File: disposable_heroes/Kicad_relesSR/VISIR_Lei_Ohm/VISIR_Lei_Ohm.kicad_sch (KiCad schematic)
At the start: 23 parts, among them J1 Raspberry PI5, J2 Fonte dc, J3 Fonte 12V, J4 Fonte 5V, K1 3572-1220-123, K2 3572-1220-123, K3 3572-1220-123, K4 3570-1331-123, K5 3570-1331-123, K6 3572-1220-123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

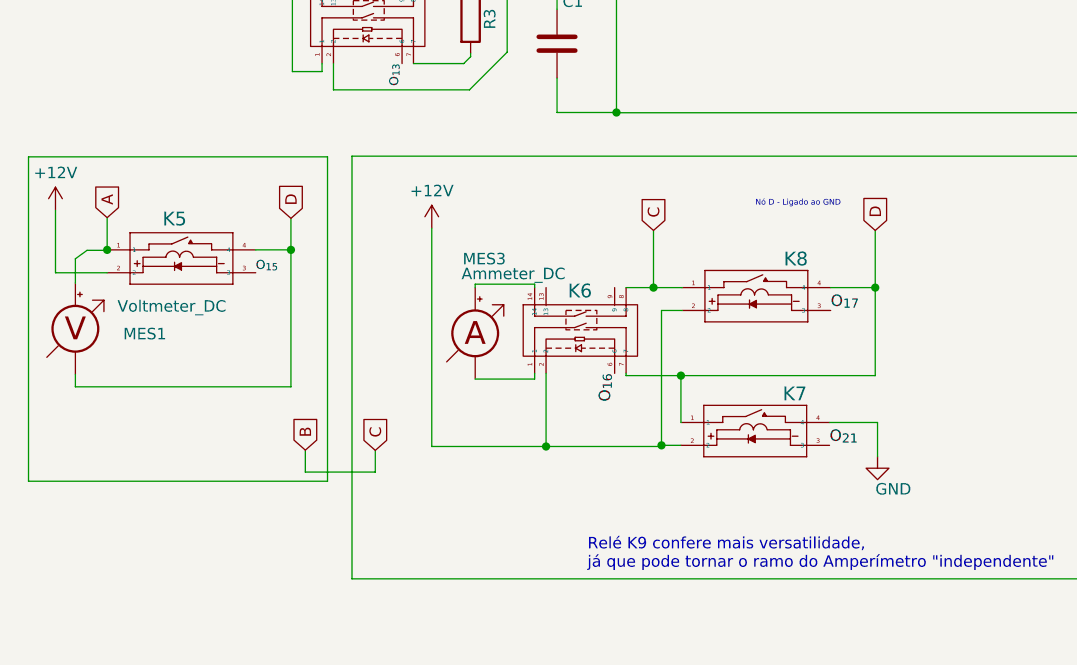
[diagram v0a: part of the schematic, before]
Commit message: Voltage/Current done Graphic interface NOT done
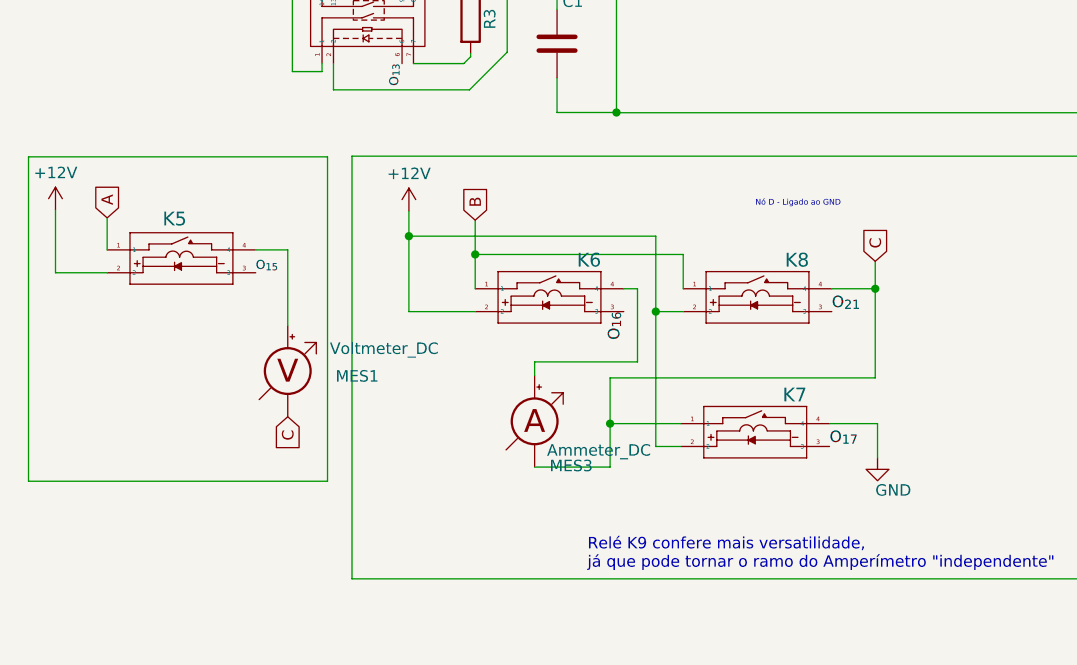
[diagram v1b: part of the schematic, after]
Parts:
- removed K6: 3572-1220-123, 3572-1220-053:RELAY8_3572-1220-053_COM, symbol 3572-1220-123:3572-1220-123
- added K6: 3570-1331-123, 3570-1220-123:SIP_3570-1331_COM, symbol 3570-1331-123:3570-1331-123
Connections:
- net +12V: now also K6.2
- net A: no longer MES1.2 (+)
- net B: now also K6.1
- net D: no longer K5.4, K7.1, K8.4, MES1.1 (-)
- net O_{16}: now also K6.3
- net O_{17}: now also K7.3; no longer K8.3
- net O_{21}: now also K8.3; no longer K7.3
- net C: now reaches MES3.1 (-)
- net C: now also K7.1, K8.4, MES1.1 (-)
- net at MES3.2 (+): now also K6.4
- new net: K5.4, MES1.2 (+)
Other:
- moved on the sheet: MES1, MES3

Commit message: update kicad
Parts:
- C1, C2: footprint (none) -> Capacitor_THT:C_Disc_D5.0mm_W2.5mm_P2.50mm
- K1, K2, K3: footprint 3572-1220-053:RELAY8_3572-1220-053_COM -> rele_DPST_tese:RELAY8_3572-1220-053_COM
- K4, K5, K6, K7, K8: footprint 3570-1220-123:SIP_3570-1331_COM -> rele_SPST_tese:SIP_3570-1331_COM
- U1, U4: footprint 74HC595N_112:DIP254P762X420-16 -> Package_DIP:DIP-16_W10.16mm
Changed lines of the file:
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@@
       (effects (font (size 1.524 1.524)) hide)
     )
-    (property "Footprint" "3570-1220-123:SIP_3570-1331_COM" (at 10.287 105.918 0)
+    (property "Footprint" "rele_SPST_tese:SIP_3570-1331_COM" (at 10.287 105.918 0)
       (effects (font (size 1.27 1.27) italic) hide)
     )
@@
       (effects (font (size 1.524 1.524)) (justify left) hide)
     )
-    (property "Footprint" "3572-1220-053:RELAY8_3572-1220-053_COM" (at 23.241 62.865 0)
+    (property "Footprint" "rele_DPST_tese:RELAY8_3572-1220-053_COM" (at 23.241 62.865 0)
       (effects (font (size 1.27 1.27) italic) hide)
     )
@@
       (effects (font (size 1.524 1.524)) hide)
     )
-    (property "Footprint" "3570-1220-123:SIP_3570-1331_COM" (at 51.181 110.236 0)
+    (property "Footprint" "rele_SPST_tese:SIP_3570-1331_COM" (at 51.181 110.236 0)
       (effects (font (size 1.27 1.27) italic) hide)
     )
@@
       (effects (font (size 1.27 1.27)) (justify left))
     )
-    (property "Footprint" "" (at 73.3044 90.6272 0)
+    (property "Footprint" "Capacitor_THT:C_Disc_D5.0mm_W2.5mm_P2.50mm" (at 73.3044 90.6272 0)
       (effects (font (size 1.27 1.27)) hide)
     )
@@
       (effects (font (size 1.524 1.524)) hide)
     )
-    (property "Footprint" "3570-1220-123:SIP_3570-1331_COM" (at 9.398 36.83 0)
+    (property "Footprint" "rele_SPST_tese:SIP_3570-1331_COM" (at 9.398 36.83 0)
       (effects (font (size 1.27 1.27) italic) hide)
     )
@@
       (effects (font (size 1.524 1.524)) (justify left) hide)
     )
-    (property "Footprint" "3572-1220-053:RELAY8_3572-1220-053_COM" (at 23.368 24.384 0)
+    (property "Footprint" "rele_DPST_tese:RELAY8_3572-1220-053_COM" (at 23.368 24.384 0)
       (effects (font (size 1.27 1.27) italic) hide)
     )
@@
       (effects (font (size 1.524 1.524)) (justify left) hide)
     )
-    (property "Footprint" "3572-1220-053:RELAY8_3572-1220-053_COM" (at 23.368 43.561 0)
+    (property "Footprint" "rele_DPST_tese:RELAY8_3572-1220-053_COM" (at 23.368 43.561 0)
       (effects (font (size 1.27 1.27) italic) hide)
     )
@@
       (effects (font (size 1.27 1.27)))
     )
-    (property "Footprint" "74HC595N_112:DIP254P762X420-16" (at 182.7022 54.2544 0)
+    (property "Footprint" "Package_DIP:DIP-16_W10.16mm" (at 182.7022 54.2544 0)
       (effects (font (size 1.27 1.27)) (justify bottom) hide)
     )
@@
       (effects (font (size 1.524 1.524)) hide)
     )
-    (property "Footprint" "3570-1220-123:SIP_3570-1331_COM" (at 74.041 125.222 0)
+    (property "Footprint" "rele_SPST_tese:SIP_3570-1331_COM" (at 74.041 125.222 0)
       (effects (font (size 1.27 1.27) italic) hide)
     )
@@
       (effects (font (size 1.27 1.27)))
     )
-    (property "Footprint" "74HC595N_112:DIP254P762X420-16" (at 97.917 54.356 0)
+    (property "Footprint" "Package_DIP:DIP-16_W10.16mm" (at 97.917 54.356 0)
       (effects (font (size 1.27 1.27)) (justify bottom) hide)
     )
@@
       (effects (font (size 1.27 1.27)) (justify left))
     )
-    (property "Footprint" "" (at 158.75 89.2556 0)
+    (property "Footprint" "Capacitor_THT:C_Disc_D5.0mm_W2.5mm_P2.50mm" (at 158.75 89.2556 0)
       (effects (font (size 1.27 1.27)) hide)
     )
@@
       (effects (font (size 1.524 1.524)) hide)
     )
-    (property "Footprint" "3570-1220-123:SIP_3570-1331_COM" (at 74.295 110.236 0)
-      (effects (font (size 1.27 1.27) italic) hide)
-    )
+    (property "Footprint" "rele_SPST_tese:SIP_3570-1331_COM" (at 74.295 110.236 0)
+      (effects (font (size 1.27 1.27) italic) hide)
+    )
